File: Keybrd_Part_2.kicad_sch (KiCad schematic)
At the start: 0 parts

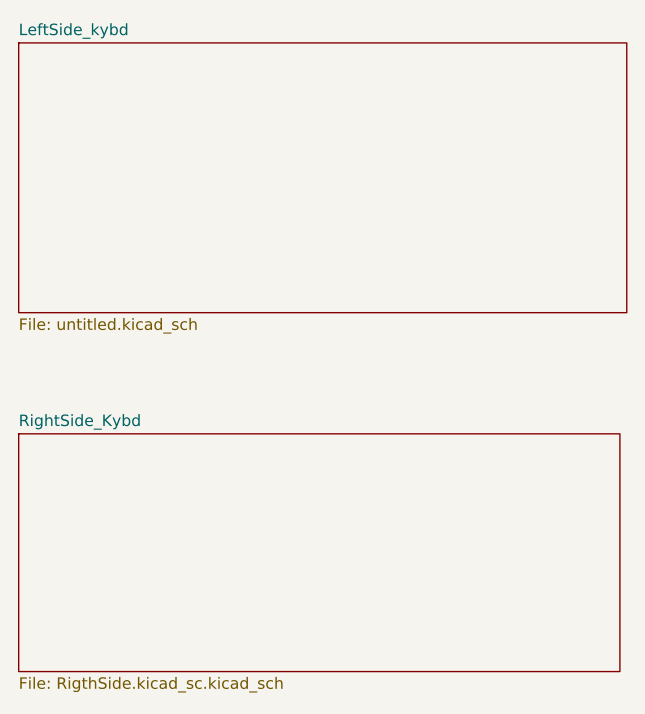
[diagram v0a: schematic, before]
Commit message: Added USBC interconnect
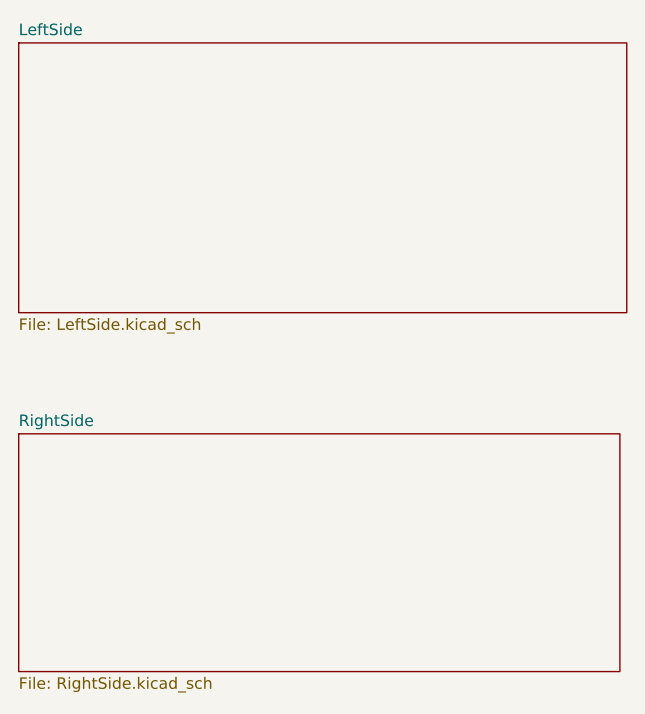
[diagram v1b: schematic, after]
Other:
- sheet LeftSide_kybd renamed LeftSide
- sheet RightSide_Kybd renamed RightSide
- sheet LeftSide: file untitled.kicad_sch -> LeftSide.kicad_sch
- sheet RightSide: file RigthSide.kicad_sc.kicad_sch -> RightSide.kicad_sch
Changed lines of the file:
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@@
 (kicad_sch
-	(version 20250114)
+	(version 20260306)
 	(generator "eeschema")
-	(generator_version "9.0")
+	(generator_version "10.0")
 	(paper "A4")
 	(sheet
@@
 		)
 		(fill
-			(color 0 0 0 0.0000)
+			(color 0 0 0 0)
 		)
-		(property "Sheetname" "LeftSide_kybd"
+		(property "Sheetname" "LeftSide"
 			(at 54.356 68.8844 0)
+			(show_name no)
+			(do_not_autoplace no)
 			(effects
 				(font
@@
 			)
 		)
-		(property "Sheetfile" "untitled.kicad_sch"
+		(property "Sheetfile" "LeftSide.kicad_sch"
 			(at 54.356 100.1526 0)
+			(show_name no)
+			(do_not_autoplace no)
 			(effects
 				(font
@@
 		)
 		(fill
-			(color 0 0 0 0.0000)
+			(color 0 0 0 0)
 		)
-		(property "Sheetname" "RightSide_Kybd"
+		(property "Sheetname" "RightSide"
 			(at 54.356 112.3184 0)
+			(show_name no)
+			(do_not_autoplace no)
 			(effects
 				(font
@@
 			)
 		)
-		(property "Sheetfile" "RigthSide.kicad_sc.kicad_sch"
+		(property "Sheetfile" "RightSide.kicad_sch"
 			(at 54.356 140.0306 0)
+			(show_name no)
+			(do_not_autoplace no)
 			(effects
 				(font
